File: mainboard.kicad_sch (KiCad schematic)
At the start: 28 parts, among them J1 terminal_led-strip, J2 header_rotary-encoder, J4 header_pi, J5 power_input, J6 AudioJack2, Q1 IRF9540N, SW1 power_switch, U1 OPA2277, U2 MSGEQ7, U4 logic-level-converter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

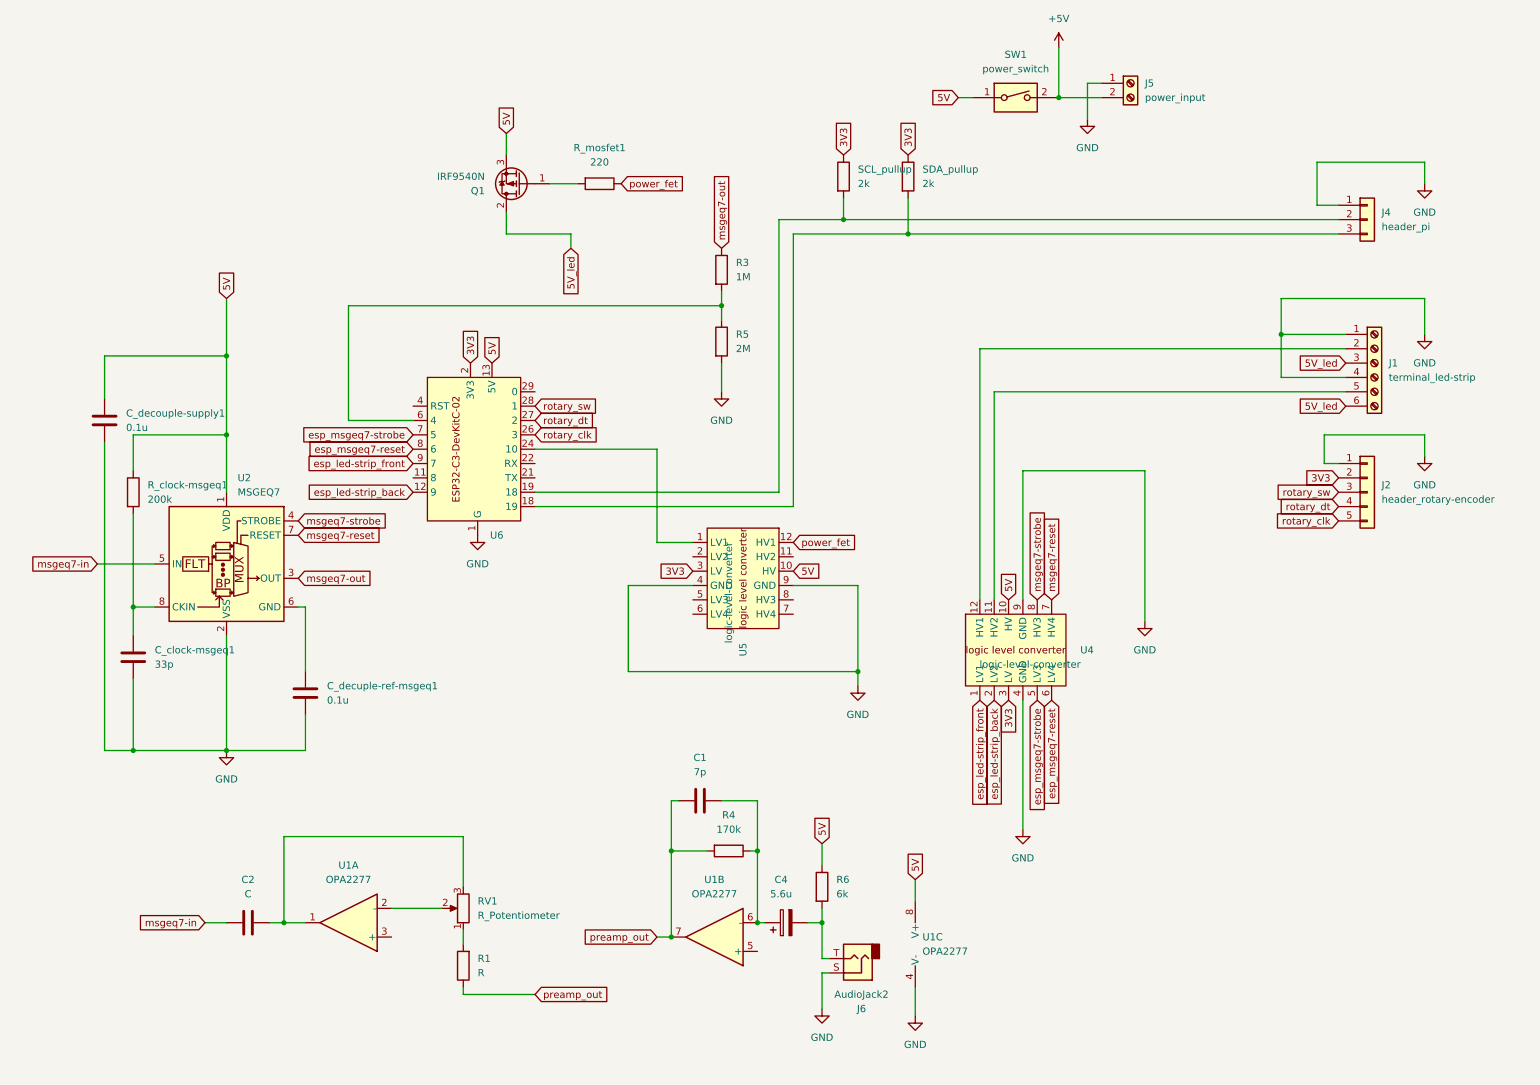
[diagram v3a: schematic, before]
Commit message: add referece voltage to opamps
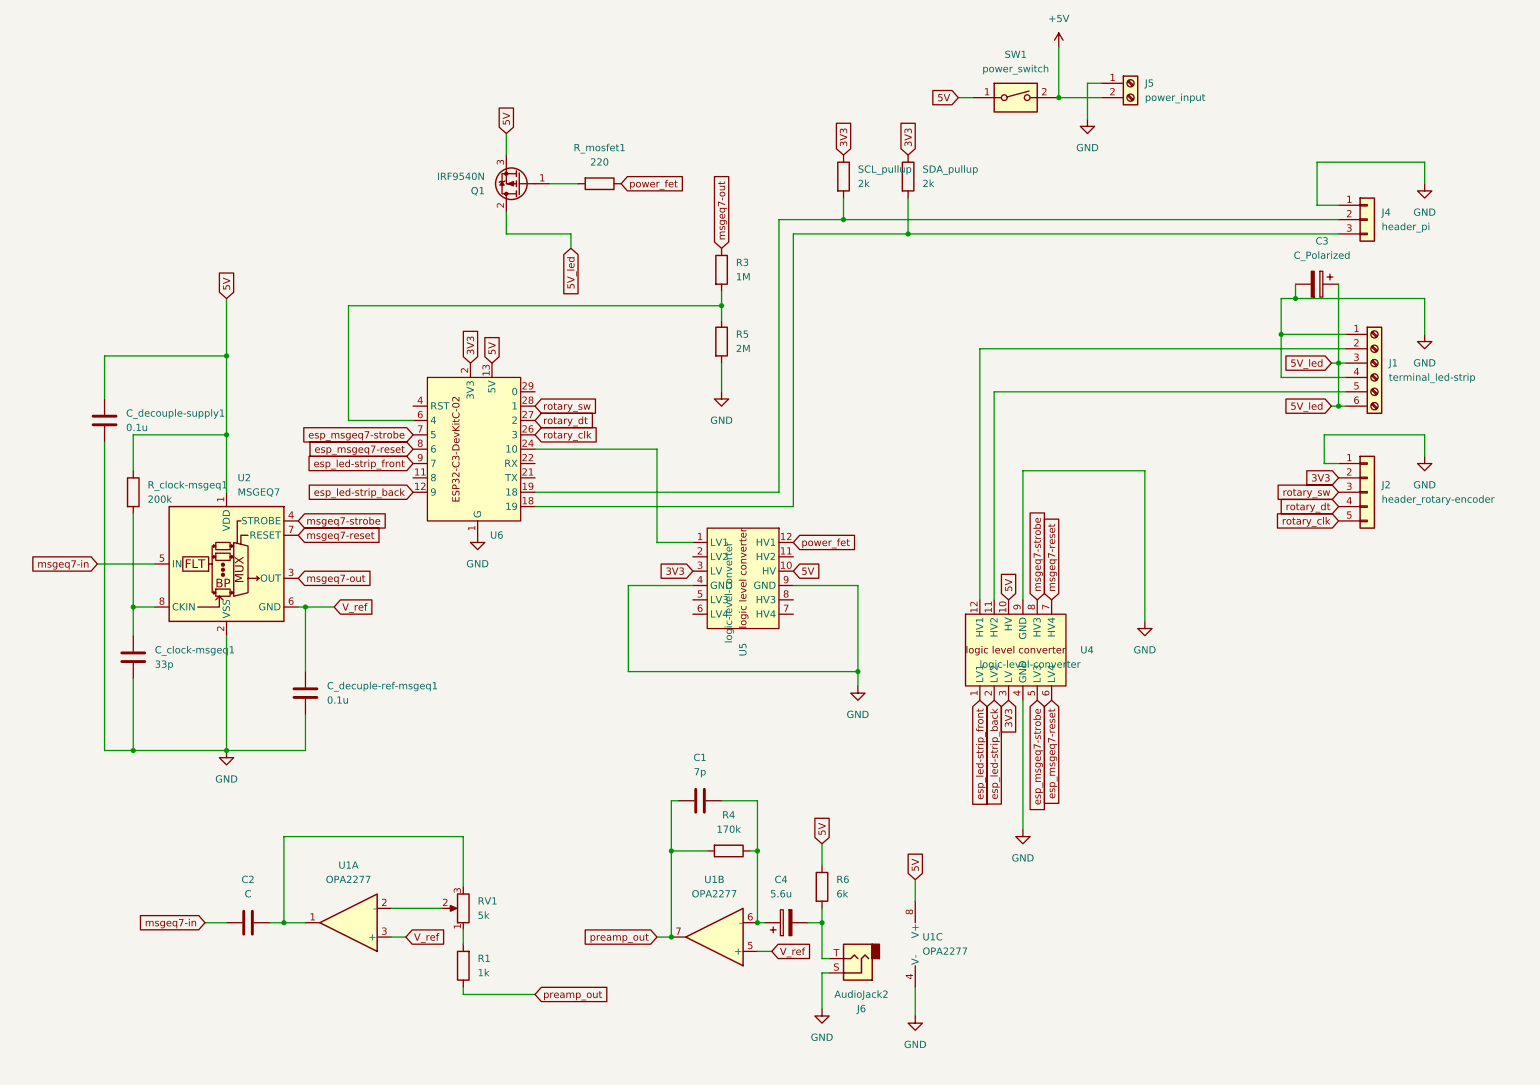
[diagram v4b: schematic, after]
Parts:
- added C3: C_Polarized, symbol Device:C_Polarized
- R1: value R -> 1k
- RV1: value R_Potentiometer -> 5k; footprint (none) -> Potentiometer_THT:Potentiometer_Piher_PT-10-V10_Vertical
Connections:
- net 5V_led: now also C3.1
- net GND: now also C3.2
- net V_ref: now reaches C_decuple-ref-msgeq1.1, U2.6 (GND)
- net V_ref: now also U1.3 (+), U1.5 (+)
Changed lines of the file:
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@@
   (junction (at 25.4 146.05) (diameter 0) (color 0 0 0 0)
   )
+  (junction (at 238.76 85.09) (diameter 0) (color 0 0 0 0)
+  )
   (junction (at 120.65 163.83) (diameter 0) (color 0 0 0 0)
   )
+  (junction (at 55.88 120.65) (diameter 0) (color 0 0 0 0)
+  )
   (junction (at 147.32 176.53) (diameter 0) (color 0 0 0 0)
   )
@@
   (junction (at 41.91 90.17) (diameter 0) (color 0 0 0 0)
   )
+  (junction (at 238.76 77.47) (diameter 0) (color 0 0 0 0)
+  )
+  (junction (at 231.14 66.04) (diameter 0) (color 0 0 0 0)
+  )
   (junction (at 25.4 120.65) (diameter 0) (color 0 0 0 0)
   )
@@
     (stroke (width 0) (type default))
   )
+  (wire (pts (xy 238.76 85.09) (xy 240.03 85.09))
+    (stroke (width 0) (type default))
+  )
   (wire (pts (xy 142.24 116.84) (xy 153.67 116.84))
     (stroke (width 0) (type default))
@@
     (stroke (width 0) (type default))
   )
+  (wire (pts (xy 238.76 63.5) (xy 238.76 77.47))
+    (stroke (width 0) (type default))
+  )
   (wire (pts (xy 129.54 64.77) (xy 129.54 67.31))
     (stroke (width 0) (type default))
@@
     (stroke (width 0) (type default))
   )
+  (wire (pts (xy 135.89 181.61) (xy 138.43 181.61))
+    (stroke (width 0) (type default))
+  )
   (wire (pts (xy 142.24 54.61) (xy 142.24 102.87))
     (stroke (width 0) (type default))
   )
+  (wire (pts (xy 71.12 179.07) (xy 73.66 179.07))
+    (stroke (width 0) (type default))
+  )
   (wire (pts (xy 20.32 146.05) (xy 25.4 146.05))
     (stroke (width 0) (type default))
@@
     (stroke (width 0) (type default))
   )
+  (wire (pts (xy 55.88 120.65) (xy 60.96 120.65))
+    (stroke (width 0) (type default))
+  )
   (wire (pts (xy 38.1 176.53) (xy 41.91 176.53))
     (stroke (width 0) (type default))
   )
+  (wire (pts (xy 238.76 77.47) (xy 240.03 77.47))
+    (stroke (width 0) (type default))
+  )
   (wire (pts (xy 118.11 179.07) (xy 120.65 179.07))
     (stroke (width 0) (type default))
@@
     (stroke (width 0) (type default))
   )
+  (wire (pts (xy 231.14 63.5) (xy 231.14 66.04))
+    (stroke (width 0) (type default))
+  )
+  (wire (pts (xy 238.76 77.47) (xy 238.76 85.09))
+    (stroke (width 0) (type default))
+  )
   (wire (pts (xy 55.88 146.05) (xy 41.91 146.05))
     (stroke (width 0) (type default))
@@
     (stroke (width 0) (type default))
   )
+  (wire (pts (xy 231.14 66.04) (xy 254 66.04))
+    (stroke (width 0) (type default))
+  )
   (wire (pts (xy 238.76 49.53) (xy 234.95 49.53))
     (stroke (width 0) (type default))
   )
-  (wire (pts (xy 228.6 66.04) (xy 254 66.04))
+  (wire (pts (xy 228.6 66.04) (xy 231.14 66.04))
     (stroke (width 0) (type default))
   )
@@
     (stroke (width 0) (type default))
   )
+  (wire (pts (xy 237.49 85.09) (xy 238.76 85.09))
+    (stroke (width 0) (type default))
+  )
   (wire (pts (xy 52.07 161.29) (xy 83.82 161.29))
     (stroke (width 0) (type default))
   )
+  (wire (pts (xy 237.49 77.47) (xy 238.76 77.47))
+    (stroke (width 0) (type default))
+  )
   (wire (pts (xy 196.85 27.94) (xy 194.31 27.94))
     (stroke (width 0) (type default))
@@
     )
   )
+  (global_label "V_ref" (shape input) (at 138.43 181.61 0) (fields_autoplaced)
+    (effects (font (size 1.27 1.27)) (justify left))
+    (property "Intersheetrefs" "${INTERSHEET_REFS}" (at 146.0719 181.61 0)
+      (effects (font (size 1.27 1.27)) (justify left) hide)
+    )
+  )
   (global_label "3V3" (shape input) (at 238.76 97.79 180) (fields_autoplaced)
     (effects (font (size 1.27 1.27)) (justify right))
@@
     )
   )
-  (global_label "5V_led" (shape input) (at 240.03 77.47 180) (fields_autoplaced)
-    (effects (font (size 1.27 1.27)) (justify right))
-    (property "Intersheetrefs" "${INTERSHEET_REFS}" (at 230.8763 77.47 0)
+  (global_label "5V_led" (shape input) (at 237.49 77.47 180) (fields_autoplaced)
+    (effects (font (size 1.27 1.27)) (justify right))
+    (property "Intersheetrefs" "${INTERSHEET_REFS}" (at 228.3363 77.47 0)
       (effects (font (size 1.27 1.27)) (justify right) hide)
     )
@@
     )
   )
+  (global_label "V_ref" (shape input) (at 60.96 120.65 0) (fields_autoplaced)
+    (effects (font (size 1.27 1.27)) (justify left))
+    (property "Intersheetrefs" "${INTERSHEET_REFS}" (at 68.6019 120.65 0)
+      (effects (font (size 1.27 1.27)) (justify left) hide)
+    )
+  )
   (global_label "msgeq7-strobe" (shape input) (at 54.61 105.41 0) (fields_autoplaced)
     (effects (font (size 1.27 1.27)) (justify left))
@@
     )
   )
-  (global_label "5V_led" (shape input) (at 240.03 85.09 180) (fields_autoplaced)
-    (effects (font (size 1.27 1.27)) (justify right))
-    (property "Intersheetrefs" "${INTERSHEET_REFS}" (at 230.8763 85.09 0)
+  (global_label "5V_led" (shape input) (at 237.49 85.09 180) (fields_autoplaced)
+    (effects (font (size 1.27 1.27)) (justify right))
+    (property "Intersheetrefs" "${INTERSHEET_REFS}" (at 228.3363 85.09 0)
       (effects (font (size 1.27 1.27)) (justify right) hide)
     )
@@
     (effects (font (size 1.27 1.27)) (justify left))
     (property "Intersheetrefs" "${INTERSHEET_REFS}" (at 187.96 102.7877 90)
+      (effects (font (size 1.27 1.27)) (justify left) hide)
+    )
+  )
+  (global_label "V_ref" (shape input) (at 73.66 179.07 0) (fields_autoplaced)
+    (effects (font (size 1.27 1.27)) (justify left))
+    (property "Intersheetrefs" "${INTERSHEET_REFS}" (at 81.3019 179.07 0)
       (effects (font (size 1.27 1.27)) (justify left) hide)
     )
@@
       (effects (font (size 1.27 1.27)) (justify right))
     )
-    (property "Value" "R" (at 86.36 185.42 0)
+    (property "Value" "1k" (at 86.36 185.42 0)
       (effects (font (size 1.27 1.27)) (justify right))
     )
@@
     )
   )
+  (symbol (lib_id "Device:C_Polarized") (at 234.95 63.5 270) (unit 1)
+    (in_bom yes) (on_board yes) (dnp no) (fields_autoplaced)
+    (property "Reference" "C3" (at 235.839 55.88 90)
+      (effects (font (size 1.27 1.27)))
+    )
+    (property "Value" "C_Polarized" (at 235.839 58.42 90)
+      (effects (font (size 1.27 1.27)))
+    )
+    (property "Footprint" "" (at 231.14 64.4652 0)
+      (effects (font (size 1.27 1.27)) hide)
+    )
+    (property "Datasheet" "~" (at 234.95 63.5 0)
+      (effects (font (size 1.27 1.27)) hide)
+    )
+    (pin "1")
+    (pin "2")
+    (instances
+      (project "mainboard"
+        (path "/3161c04b-751c-4104-8356-8b48a6ef4a37"
+          (reference "C3") (unit 1)
+        )
+      )
+    )
+  )
   (symbol (lib_id "Amplifier_Operational:OPA2277") (at 63.5 176.53 180) (unit 1)
     (in_bom yes) (on_board yes) (dnp no) (fields_autoplaced)
@@
       (effects (font (size 1.27 1.27)) (justify right))
     )
-    (property "Value" "R_Potentiometer" (at 86.36 175.26 0)
+    (property "Value" "5k" (at 86.36 175.26 0)
       (effects (font (size 1.27 1.27)) (justify right))
     )
-    (property "Footprint" "" (at 83.82 173.99 0)
-      (effects (font (size 1.27 1.27)) hide)
-    )
+    (property "Footprint" "Potentiometer_THT:Potentiometer_Piher_PT-10-V10_Vertical" (at 83.82 173.99 0)
+      (effects (font (size 1.27 1.27)) hide)
+    )

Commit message: add fields for JLC manufacturing
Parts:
- C1, C4, C_clock-msgeq1, C_decouple-supply1, C_decuple-ref-msgeq1: JLC (none) -> 0805
- C2: footprint (none) -> Capacitor_SMD:C_0805_2012Metric_Pad1.18x1.45mm_HandSolder; JLC (none) -> 0805
- C3: footprint (none) -> Capacitor_THT:CP_Radial_D8.0mm_P5.00mm
- R1: footprint (none) -> Resistor_SMD:R_0805_2012Metric_Pad1.20x1.40mm_HandSolder; JLC (none) -> 0805
- R3, R4, R5, R6, R_clock-msgeq1, R_mosfet1, SCL_pullup, SDA_pullup: footprint Resistor_SMD:R_0603_1608Metric_Pad0.98x0.95mm_HandSolder -> Resistor_SMD:R_0805_2012Metric_Pad1.20x1.40mm_HandSolder; JLC (none) -> 0805

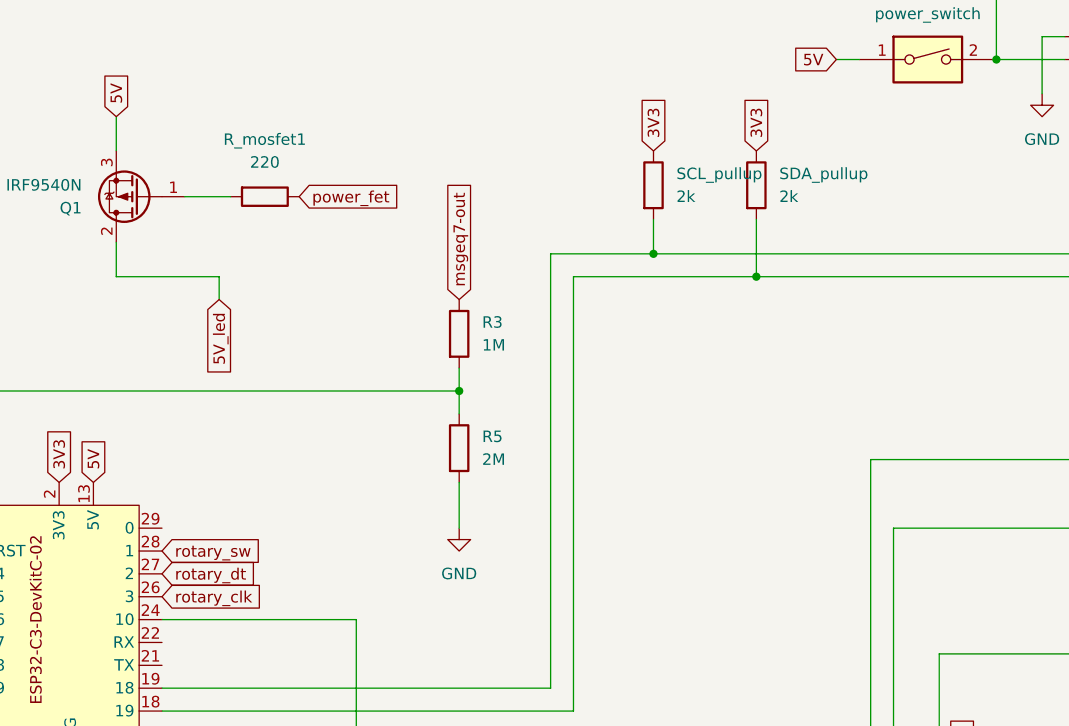
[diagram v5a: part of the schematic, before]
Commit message: start routing tracks
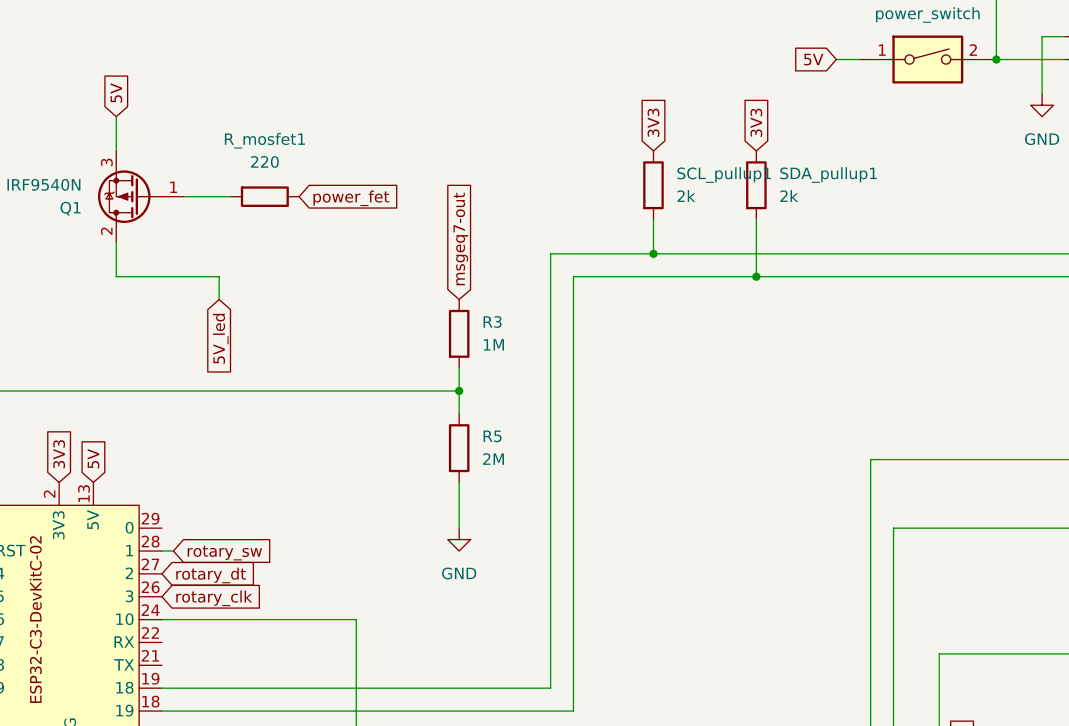
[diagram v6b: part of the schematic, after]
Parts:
- C4: footprint Capacitor_Tantalum_SMD:CP_EIA-7343-31_Kemet-D_Pad2.25x2.55mm_HandSolder -> Capacitor_THT:CP_Radial_D5.0mm_P2.50mm
- J4: footprint (none) -> Connector_PinHeader_2.54mm:PinHeader_1x03_P2.54mm_Vertical
- U6: footprint (none) -> my_lib:esp32_c3_dev-kit-c_02
- renumbered SCL_pullup to SCL_pullup1, SDA_pullup to SDA_pullup1
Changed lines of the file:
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@@
+    (stroke (width 0) (type default))
+  )
+  (wire (pts (xy 97.79 85.09) (xy 96.52 85.09))
     (stroke (width 0) (type default))
   )
@@
     )
   )
-  (global_label "rotary_sw" (shape input) (at 96.52 85.09 0) (fields_autoplaced)
-    (effects (font (size 1.27 1.27)) (justify left))
-    (property "Intersheetrefs" "${INTERSHEET_REFS}" (at 108.3951 85.09 0)
+  (global_label "rotary_sw" (shape input) (at 97.79 85.09 0) (fields_autoplaced)
+    (effects (font (size 1.27 1.27)) (justify left))
+    (property "Intersheetrefs" "${INTERSHEET_REFS}" (at 109.6651 85.09 0)
       (effects (font (size 1.27 1.27)) (justify left) hide)
     )
@@
       (effects (font (size 1.27 1.27)))
     )
-    (property "Footprint" "Capacitor_Tantalum_SMD:CP_EIA-7343-31_Kemet-D_Pad2.25x2.55mm_HandSolder" (at 144.78 175.5648 0)
+    (property "Footprint" "Capacitor_THT:CP_Radial_D5.0mm_P2.50mm" (at 144.78 175.5648 0)
       (effects (font (size 1.27 1.27)) hide)
     )
@@
       (effects (font (size 1.27 1.27)))
     )
-    (property "Footprint" "" (at 86.36 99.06 0)
+    (property "Footprint" "my_lib:esp32_c3_dev-kit-c_02" (at 86.36 99.06 0)
       (effects (font (size 1.27 1.27)) hide)
     )
@@
   (symbol (lib_id "Device:R") (at 162.56 44.45 0) (unit 1)
     (in_bom yes) (on_board yes) (dnp no) (fields_autoplaced)
-    (property "Reference" "SDA_pullup" (at 165.1 43.18 0)
+    (property "Reference" "SDA_pullup1" (at 165.1 43.18 0)
       (effects (font (size 1.27 1.27)) (justify left))
     )
@@
       (project "mainboard"
         (path "/3161c04b-751c-4104-8356-8b48a6ef4a37"
-          (reference "SDA_pullup") (unit 1)
+          (reference "SDA_pullup1") (unit 1)
         )
       )
@@
       (effects (font (size 1.27 1.27)) (justify left))
     )
-    (property "Footprint" "" (at 243.84 52.07 0)
+    (property "Footprint" "Connector_PinHeader_2.54mm:PinHeader_1x03_P2.54mm_Vertical" (at 243.84 52.07 0)
       (effects (font (size 1.27 1.27)) hide)
     )
@@
   (symbol (lib_id "Device:R") (at 151.13 44.45 0) (unit 1)
     (in_bom yes) (on_board yes) (dnp no) (fields_autoplaced)
-    (property "Reference" "SCL_pullup" (at 153.67 43.18 0)
+    (property "Reference" "SCL_pullup1" (at 153.67 43.18 0)
       (effects (font (size 1.27 1.27)) (justify left))
     )
@@
       (project "mainboard"
         (path "/3161c04b-751c-4104-8356-8b48a6ef4a37"
-          (reference "SCL_pullup") (unit 1)
-        )
-      )
+          (reference "SCL_pullup1") (unit 1)
+        )
+      )

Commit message: route tracks and add mounting holes
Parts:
- removed U6: ~, my_lib:esp32_c3_dev-kit-c_02, symbol my_lib:esp32_c3_dev-kit-c_02
- added U3: ~, my_lib:esp32_c3_dev-kit-c_02, symbol my_lib:esp32_c3_dev-kit-c_02
- C1, C_clock-msgeq1, C_decouple-supply1, C_decuple-ref-msgeq1: footprint Capacitor_SMD:C_0603_1608Metric_Pad1.08x0.95mm_HandSolder -> Capacitor_SMD:C_0805_2012Metric_Pad1.18x1.45mm_HandSolder
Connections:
- net 3V3: now also U3.13 (3V3)
- net 5V: now also U3.14 (5V)
- net GND: now also U3.11 (GND)
- net esp_led-strip_back: now also U3.9 (GPIO9)
- net esp_led-strip_front: now also U3.7 (GPIO7)
- net esp_msgeq7-reset: now also U3.6 (GPIO6)
- net esp_msgeq7-strobe: now also U3.5 (GPIO5/(ADC2_CH0))
- net rotary_clk: now also U3.3 (GPIO3/ADC1_CH3)
- net rotary_dt: now also U3.2 (GPIO2/ADC1_CH2)
- net rotary_sw: now also U3.1 (GPIO1/ADC1_CH1)
- net at R3.2, R5.1: now also U3.4 (GPIO4/ADC1_CH4)
- net at J4.3 (Pin_3), SDA_pullup1.2: now also U3.19 (GPIO19/USB_D+)
- net at J4.2 (Pin_2), SCL_pullup1.2: now also U3.18 (GPIO18/USB_D-)
- net at U5.1 (LV1): now also U3.10 (GPIO10)
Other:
- moved on the sheet: R3, R5
